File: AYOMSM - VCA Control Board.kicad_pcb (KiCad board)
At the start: 2 copper layers, 19 x 99 mm, 11 parts, among them J1 SIGNAL_OUT, J2 CV1, J3 CV2, J4 SIGNAL_IN, J5 CONN_1, J6 CONN_2, SW1 SW_SPDT

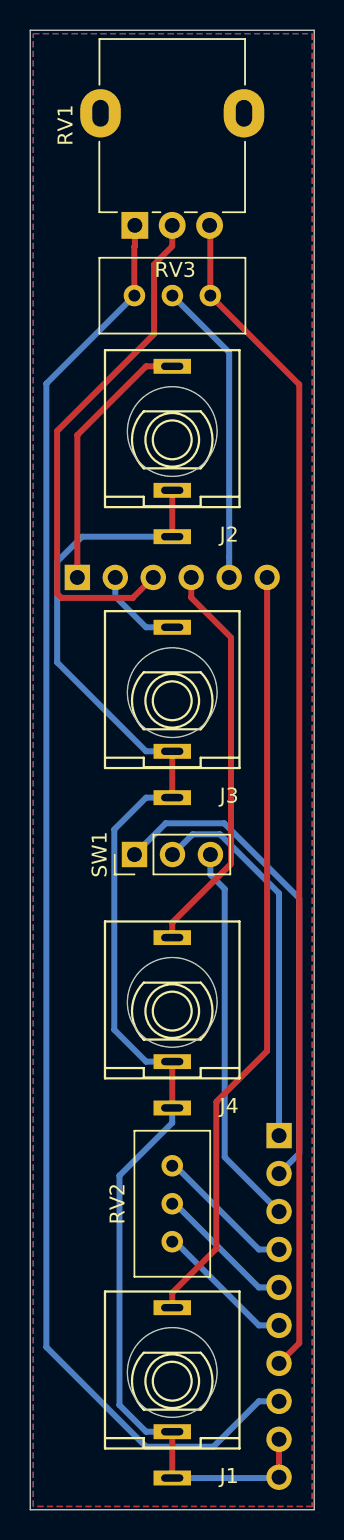
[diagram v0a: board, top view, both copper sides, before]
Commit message: Added test point for offset potentiometer
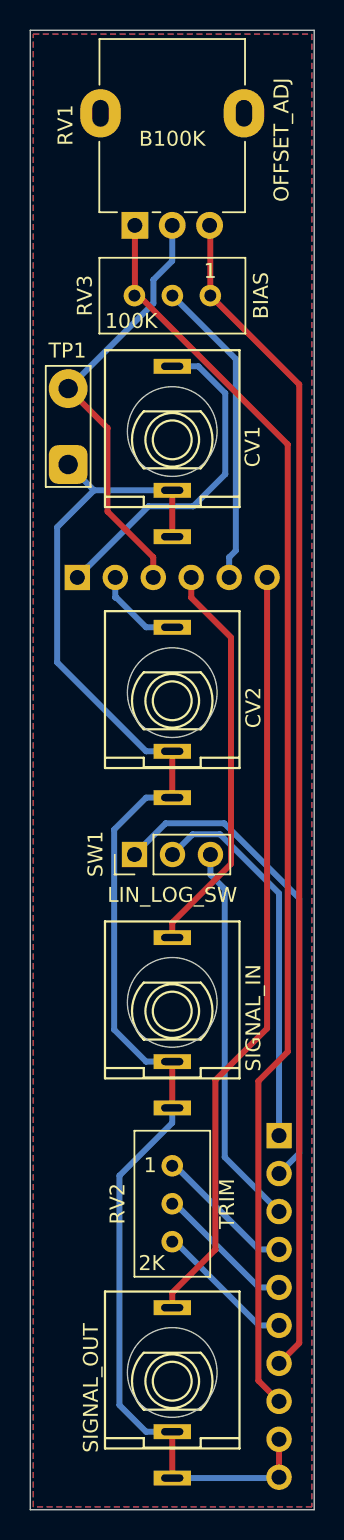
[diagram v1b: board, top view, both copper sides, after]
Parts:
- added TP1: OFFSET_ADJ_TP, TestPoint:TestPoint_2Pads_Pitch5.08mm_Drill1.3mm, F.Cu at (78.5, 83.1)
- RV1: value R_POT -> OFFSET_ADJ
- SW1: value SW_SPDT -> LIN_LOG_SW
- renumbered J2 to CV1, J3 to CV2, J4 to SIGNAL_IN, J1 to SIGNAL_OUT
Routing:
- net -12V: track 97.1 -> 84.5 mm
- net /OFFSET_ADJ: track 34.9 -> 28.8 mm
- net GND: track 95.9 -> 101.0 mm
- net /CV1: track 17.8 -> 22.5 mm
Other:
- board text added: "1"

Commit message: Updated layout and added SPDT switch model
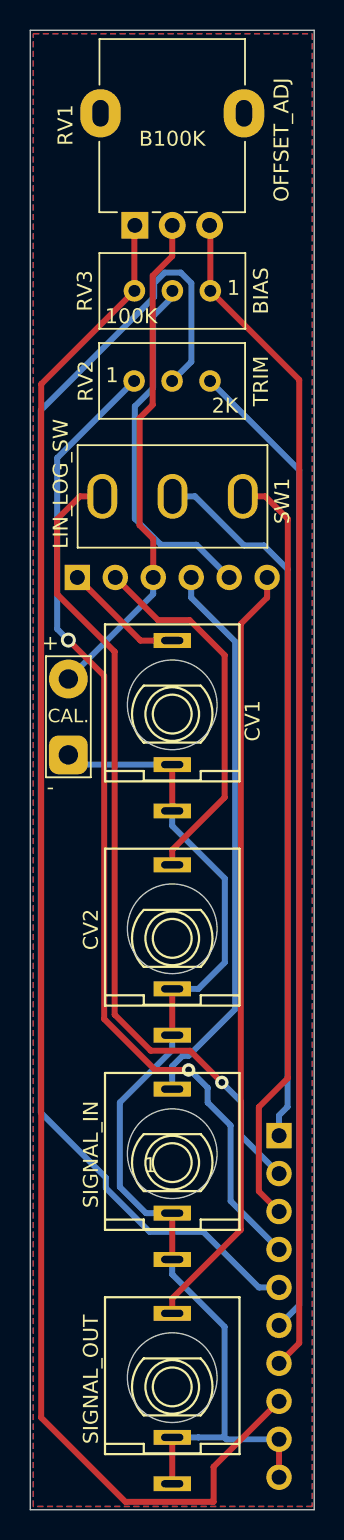
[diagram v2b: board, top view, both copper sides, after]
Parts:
- SW1: footprint Connector_PinHeader_2.54mm:PinHeader_1x03_P2.54mm_Vertical -> Custom:Mini_Toggle_Switch_SPDT_ON-ON
- moved RV2 52.6 mm to (83.0, 77.5), turned to 180 degrees
- moved SW1 24.1 mm to (85.8, 85.2), turned to 270 degrees
- moved CAL. 19.4 mm to (78.5, 102.5)
- moved CV1 18.4 mm to (85.5, 99.8)
- moved CV2 15.9 mm to (85.5, 114.8)
- moved SIGNAL_IN 10.1 mm to (85.5, 129.8)
- moved SIGNAL_OUT 0.38 mm to (85.5, 144.8)
- moved RV3 0.32 mm to (88.0, 71.4)
- renumbered TP1 to CAL.
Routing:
- net /TRIM_2: track 9.47 -> 90.0 mm
- net /TRIM_1: track 9.47 -> 67.8 mm, vias 0 -> 2
- net /TRIM_3: track 9.47 -> 66.2 mm
- net GND: track 101.0 -> 74.4 mm
- net /LOG_LIN_SW_3: track 25.8 -> 51.3 mm
- net /LOG_LIN_SW_1: track 25.5 -> 47.9 mm
- net /LOG_LIN_SW_2: track 32.9 -> 55.1 mm, vias 0 -> 1
- net -12V: track 84.5 -> 104.8 mm
- net /CV2: track 5.98 -> 25.0 mm
- net /CV1: track 22.5 -> 8.10 mm
- net /SIGNAL_IN: track 26.8 -> 37.4 mm
- net /OFFSET_ADJ: track 28.8 -> 34.0 mm
- net /BIAS: track 20.8 -> 24.2 mm
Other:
- outline, holes or cut-outs redrawn
- net class Default: via_dia 0.8 -> 1; via_drill 0.4 -> 0.6
- board text added: "+"
- board text added: "-"
- board text added: "Original Design by Ray Wilson (Music From Outer Space)"
- board text added: "Shapetaker Audio - Utility VCA Control Board (Rev 1.0)"

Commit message: Updated Thonkiconn footprints
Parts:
- SW1: value LIN_LOG_SW -> SW_SPDT
- moved CV2 0.09 mm to (85.5, 114.7)
- moved CV1 0.07 mm to (85.5, 99.8)
- renumbered CAL. to TP1
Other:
- outline, holes or cut-outs redrawn

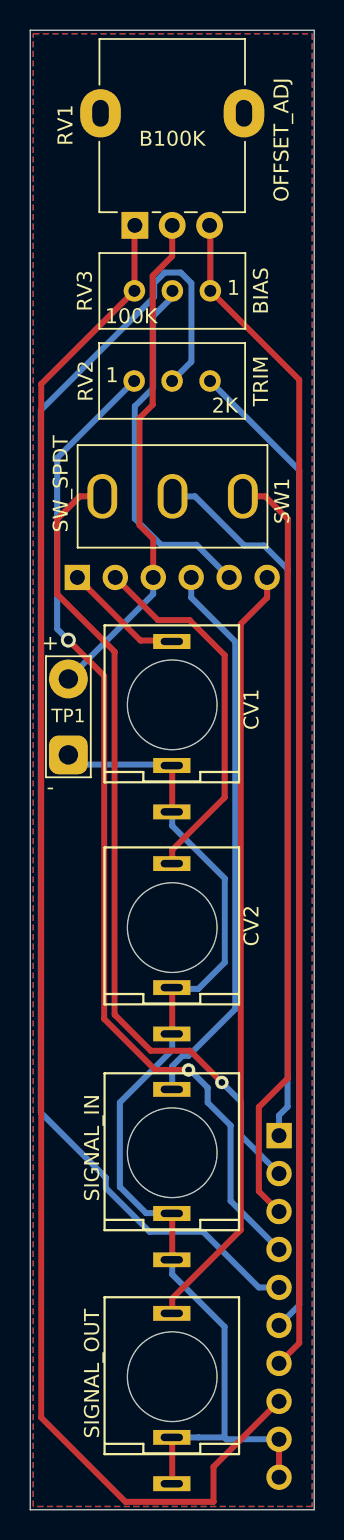
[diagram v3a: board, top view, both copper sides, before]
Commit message: Updated silkscreen
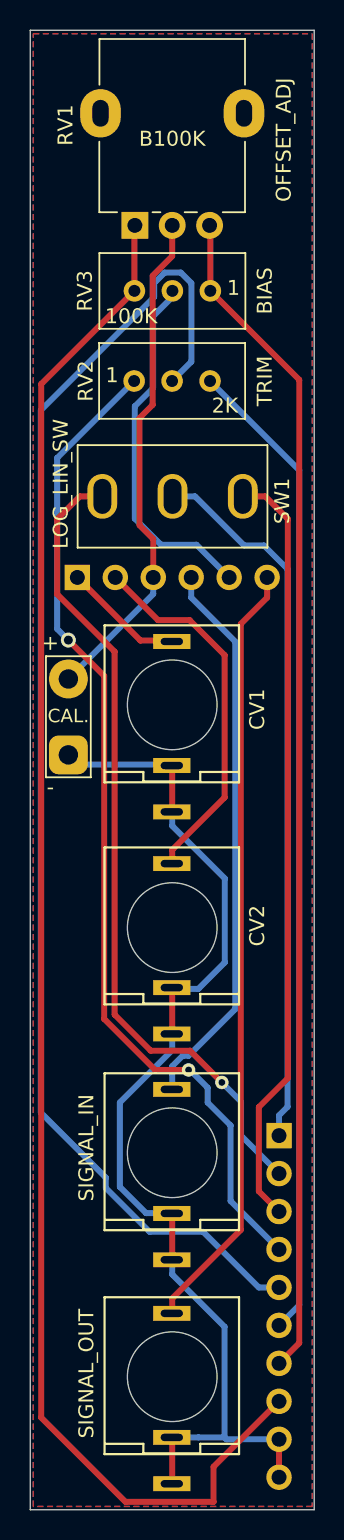
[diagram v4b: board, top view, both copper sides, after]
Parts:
- SW1: value SW_SPDT -> LOG_LIN_SW
- renumbered TP1 to CAL.
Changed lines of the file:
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@@
   (page A4)
   (layers
-    (0 F.Cu mixed)
-    (31 B.Cu mixed)
+    (0 F.Cu mixed hide)
+    (31 B.Cu mixed hide)
     (32 B.Adhes user)
     (33 F.Adhes user)
@@
     (solder_mask_min_width 0.25)
     (aux_axis_origin 0 0)
+    (grid_origin 92.964 60.833)
     (visible_elements FFFFFF7F)
     (pcbplotparams
@@
       (effects (font (size 1 1) (thickness 0.15)))
     )
-    (fp_text value TRIM (at -8.49 0 90) (layer F.SilkS)
+    (fp_text value TRIM (at -8.744 0 90) (layer F.SilkS)
       (effects (font (size 1 1) (thickness 0.15)))
     )
@@
       (effects (font (size 1 1) (thickness 0.15)))
     )
-    (fp_text value BIAS (at 3.39 0 90) (layer F.SilkS)
+    (fp_text value BIAS (at 3.644 0 90) (layer F.SilkS)
       (effects (font (size 1 1) (thickness 0.15)))
     )
@@
       (effects (font (size 1 1) (thickness 0.15)))
     )
-    (fp_text value OFFSET_ADJ (at 5.724999 9.8116 270) (layer F.SilkS)
+    (fp_text value OFFSET_ADJ (at 5.724999 9.964 270) (layer F.SilkS)
       (effects (font (size 1 1) (thickness 0.15)))
     )
@@
     (tags "CONN DEV")
     (attr virtual)
-    (fp_text reference TP1 (at 2.6035 0) (layer F.SilkS)
+    (fp_text reference CAL. (at 2.6035 0) (layer F.SilkS)
       (effects (font (size 0.9 0.9) (thickness 0.15)))
     )
@@
       (effects (font (size 1 1) (thickness 0.15)))
     )
-    (fp_text value SW_SPDT (at -0.863761 7.8105 90) (layer F.SilkS)
+    (fp_text value LOG_LIN_SW (at -0.863761 7.8105 90) (layer F.SilkS)
       (effects (font (size 1 1) (thickness 0.15)))
     )
@@
   (module Thonkiconn:thonkiconn_fuzzySi (layer F.Cu)
     (at 85.471 99.822)
-    (fp_text reference CV1 (at 5.334 -0.381 90) (layer F.SilkS)
+    (fp_text reference CV1 (at 5.715 -0.381 90) (layer F.SilkS)
       (effects (font (size 1 1) (thickness 0.15)))
     )
@@
   (module Thonkiconn:thonkiconn_fuzzySi (layer F.Cu)
     (at 85.471 114.681)
-    (fp_text reference CV2 (at 5.334 -0.762 90) (layer F.SilkS)
+    (fp_text reference CV2 (at 5.715 -0.762 90) (layer F.SilkS)
       (effects (font (size 1 1) (thickness 0.15)))
     )
@@
   (module Thonkiconn:thonkiconn_fuzzySi (layer F.Cu)
     (at 85.471 129.794)
-    (fp_text reference SIGNAL_IN (at -5.334 -1.016 90) (layer F.SilkS)
+    (fp_text reference SIGNAL_IN (at -5.715 -1.016 90) (layer F.SilkS)
       (effects (font (size 1 1) (thickness 0.15)))
     )
@@
   (module Thonkiconn:thonkiconn_fuzzySi (layer F.Cu)
     (at 85.471 144.78)
-    (fp_text reference SIGNAL_OUT (at -5.334 -0.889 90) (layer F.SilkS)
-      (effects (font (size 1 1) (thickness 0.15)))
-    )
+    (fp_text reference SIGNAL_OUT (at -5.715 -0.889 90) (layer F.SilkS)
+      (effects (font (size 1 1) (thickness 0.15)))
+    )
